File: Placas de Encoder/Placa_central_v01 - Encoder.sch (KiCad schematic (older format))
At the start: 32 parts, among them J1 Conn_01x01_Female, J2 Conn_01x01_Female, J3 Conn_01x01_Female, J4 Conn_01x01_Female, J5 Conn_01x01_Female, J6 Conn_01x01_Female, U1 TCRT5000Esq, U2 LM741Esq, U3 TCRT5000Dir, U4 LM741

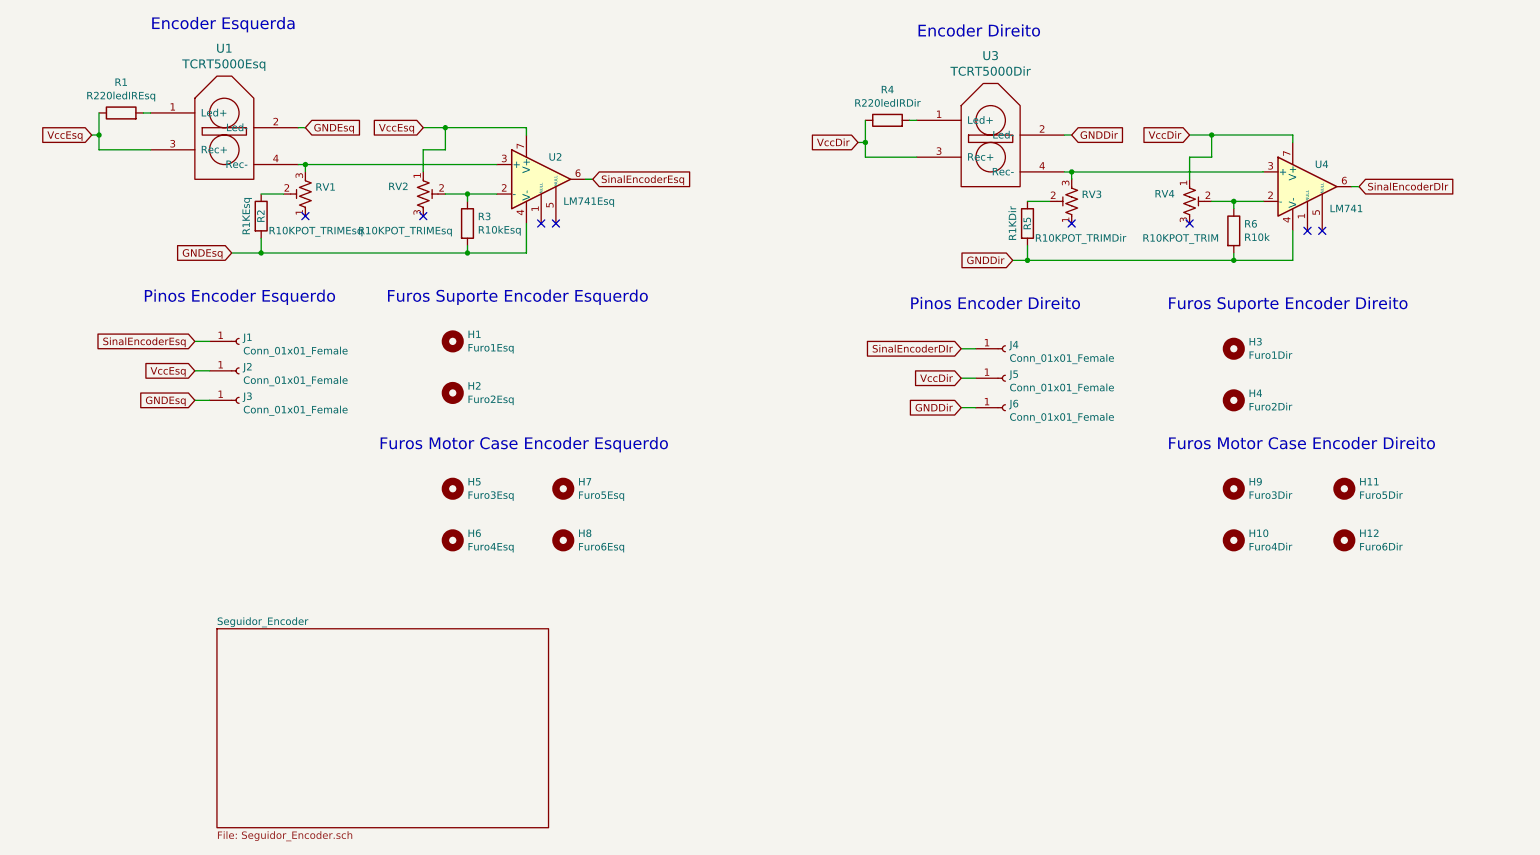
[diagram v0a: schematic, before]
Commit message: Acertos finais para documentação
Foram organizados e preparados para serem folhas em baixo de um um folha hierárquica maior, os projetos das placa de alimentação e das placas de encoder.
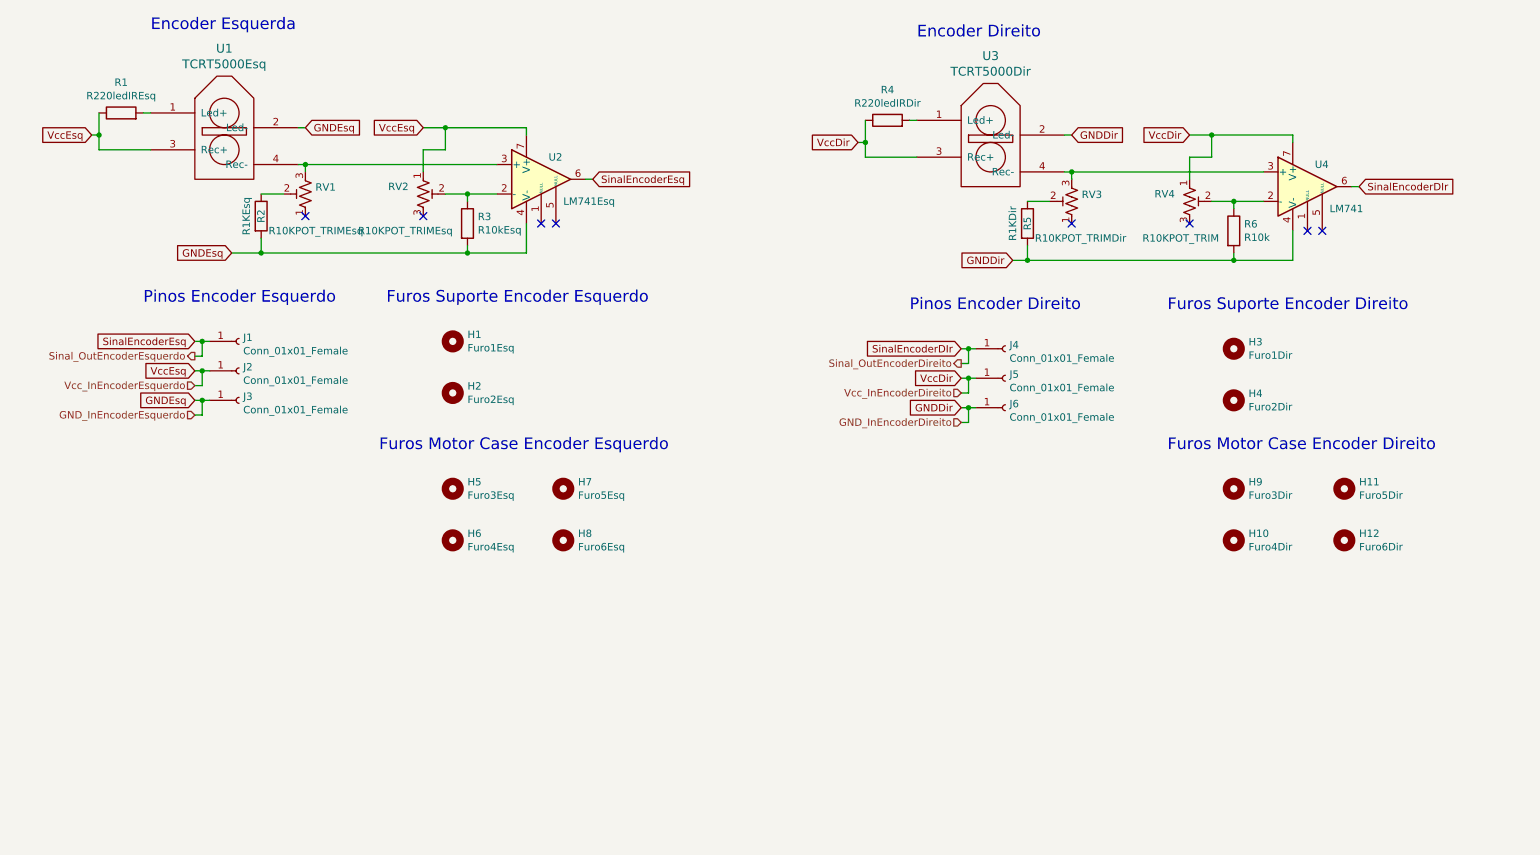
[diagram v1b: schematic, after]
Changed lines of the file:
@@
 EESchema Schematic File Version 4
-LIBS:Placa_central_v01 - Encoder-cache
-EELAYER 26 0
+EELAYER 30 0
 EELAYER END
 $Descr A4 11693 8268
 encoding utf-8
-Sheet 1 2
+Sheet 1 1
 Title ""
 Date ""
@@
 NoConn ~ 2850 2700
 Wire Wire Line
-	2100 3950 2200 3950
-Wire Wire Line
-	2100 3750 2200 3750
-Wire Wire Line
-	2100 3550 2200 3550
+	2100 3950 2150 3950
+Wire Wire Line
+	2100 3750 2150 3750
+Wire Wire Line
+	2100 3550 2150 3550
 $Comp
 L Device:R R2
@@
 NoConn ~ 8050 2750
 Wire Wire Line
-	7300 4000 7400 4000
-Wire Wire Line
-	7300 3800 7400 3800
-Wire Wire Line
-	7300 3600 7400 3600
+	7300 4000 7350 4000
+Wire Wire Line
+	7300 3800 7350 3800
+Wire Wire Line
+	7300 3600 7350 3600
 $Comp
 L Device:R R5
@@
 	1    0    0    -1
 $EndComp
-$Sheet
-S 2250 5500 2250 1350
-U 5D8012D5
-F0 "Seguidor_Encoder" 50
-F1 "Seguidor_Encoder.sch" 50
-$EndSheet
+Text HLabel 2100 3650 0    50   Output ~ 0
+Sinal_OutEncoderEsquerdo
+Text HLabel 2100 3850 0    50   Input ~ 0
+Vcc_InEncoderEsquerdo
+Text HLabel 2100 4050 0    50   Input ~ 0
+GND_InEncoderEsquerdo
+Text HLabel 7300 3700 0    50   Output ~ 0
+Sinal_OutEncoderDireito
+Text HLabel 7300 3900 0    50   Input ~ 0
+Vcc_InEncoderDireito
+Text HLabel 7300 4100 0    50   Input ~ 0
+GND_InEncoderDireito
+Wire Wire Line
+	2100 3650 2150 3650
+Wire Wire Line
+	2150 3650 2150 3550
+Connection ~ 2150 3550
+Wire Wire Line
+	2150 3550 2200 3550
+Wire Wire Line
+	2100 3850 2150 3850
+Wire Wire Line
+	2150 3850 2150 3750
+Connection ~ 2150 3750
+Wire Wire Line
+	2150 3750 2200 3750
+Wire Wire Line
+	2100 4050 2150 4050
+Wire Wire Line
+	2150 4050 2150 3950
+Connection ~ 2150 3950
+Wire Wire Line
+	2150 3950 2200 3950
+Wire Wire Line
+	7300 3700 7350 3700
+Wire Wire Line
+	7350 3700 7350 3600
+Connection ~ 7350 3600
+Wire Wire Line
+	7350 3600 7400 3600
+Wire Wire Line
+	7300 3900 7350 3900
+Wire Wire Line
+	7350 3900 7350 3800
+Connection ~ 7350 3800
+Wire Wire Line
+	7350 3800 7400 3800
+Wire Wire Line
+	7300 4100 7350 4100
+Wire Wire Line
+	7350 4100 7350 4000
+Connection ~ 7350 4000
+Wire Wire Line
+	7350 4000 7400 4000
 $EndSCHEMATC

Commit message: Ajuste final
Acertado a placa central, verificado conflitos de etiquetas hierárquicas, ligados os projeto um no outro, ajustado o projeto principal e linkado todos as placas ao projeto principal.
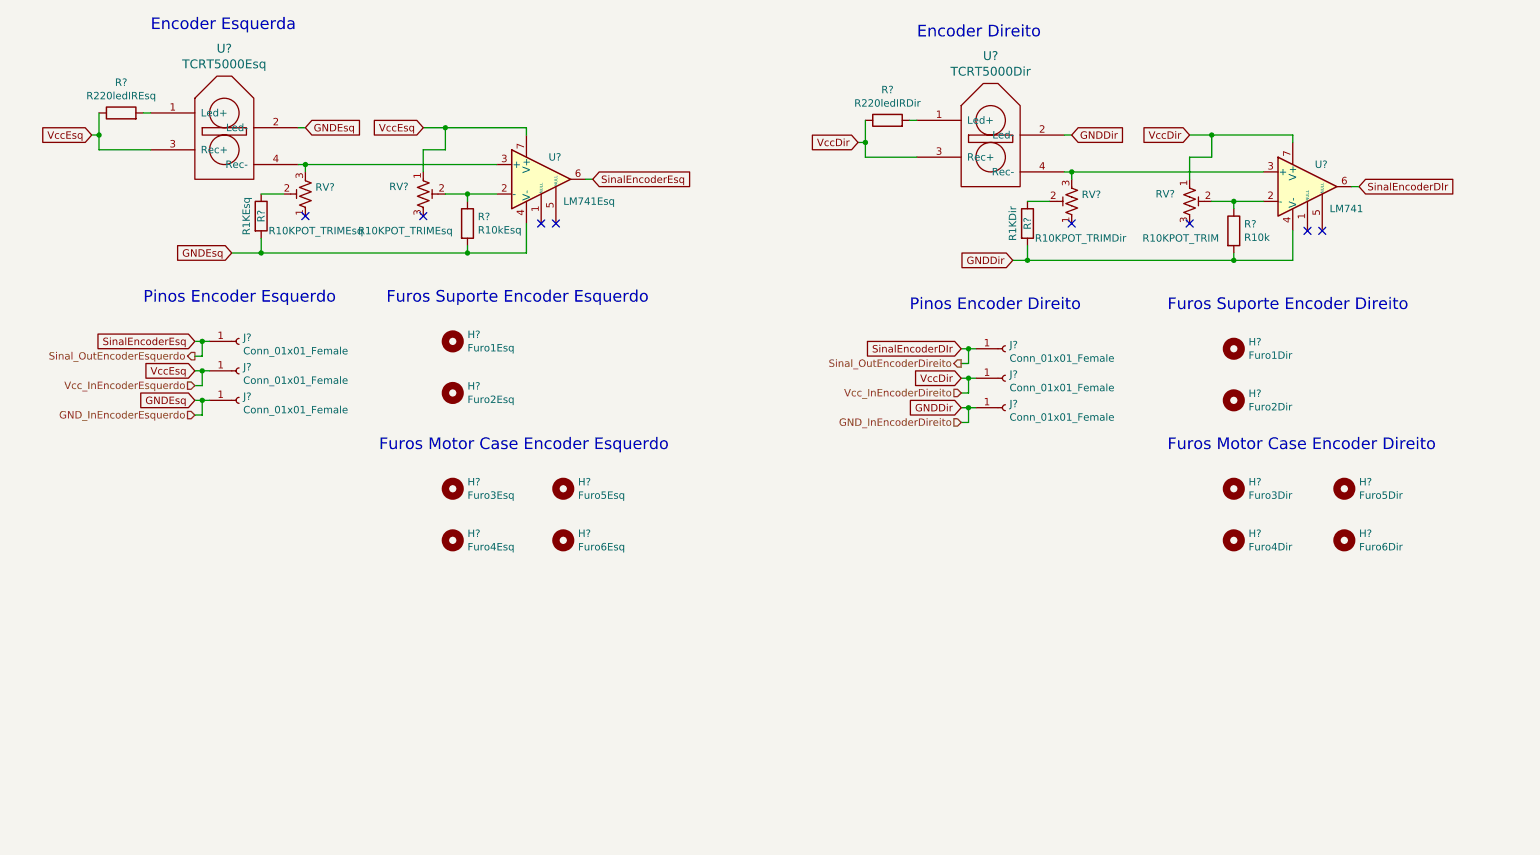
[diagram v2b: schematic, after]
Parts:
- renumbered H1 to H?, H2 to H?, H3 to H?, H4 to H?, H5 to H?, H6 to H?, H7 to H?, H8 to H?, H9 to H?, H10 to H?, H11 to H?, H12 to H?, J2 to J?, J1 to J?, J3 to J?, J5 to J?, J4 to J?, J6 to J?, R1 to R?, R3 to R?, R2 to R?, R4 to R?, R6 to R?, R5 to R?, RV2 to RV?, RV1 to RV?, RV4 to RV?, RV3 to RV?, U1 to U?, U2 to U?, U3 to U?, U4 to U?
